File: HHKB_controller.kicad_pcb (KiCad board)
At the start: 2 copper layers, 141.5 x 36 mm, 94 parts, among them CN1 JP, CN2 PRO2, J1 USB_mini_micro_B, P1 GND, P10 CONN_1, P100 LIPO, P11 CONN_1, P110 CONN_1, P111 CONN_1, P112 CONN_1, P113 CONN_1, P114 CONN_1, P115 CONN_1, P12 CONN_1, P13 CONN_1, P14 CONN_1, P15 CONN_1, P2 D+, P3 D-, P4 VUSB, P5 PD1, P6 PD0, P7 GND, P8 CONN_3X2, P9 CONN_1, Q1 Nch, Q10 Nch, Q2 Nch, Q3 Nch, Q4 Pch, Q5 Pch, SW1 SW_PUSH, SW2 SW_DPDT, U1 ATMEGA32U4, U2 MIC5504-3.3YMTR, U3 NCP1402SN50, U4 MCP73832, U5 RN42, X1 16MHz

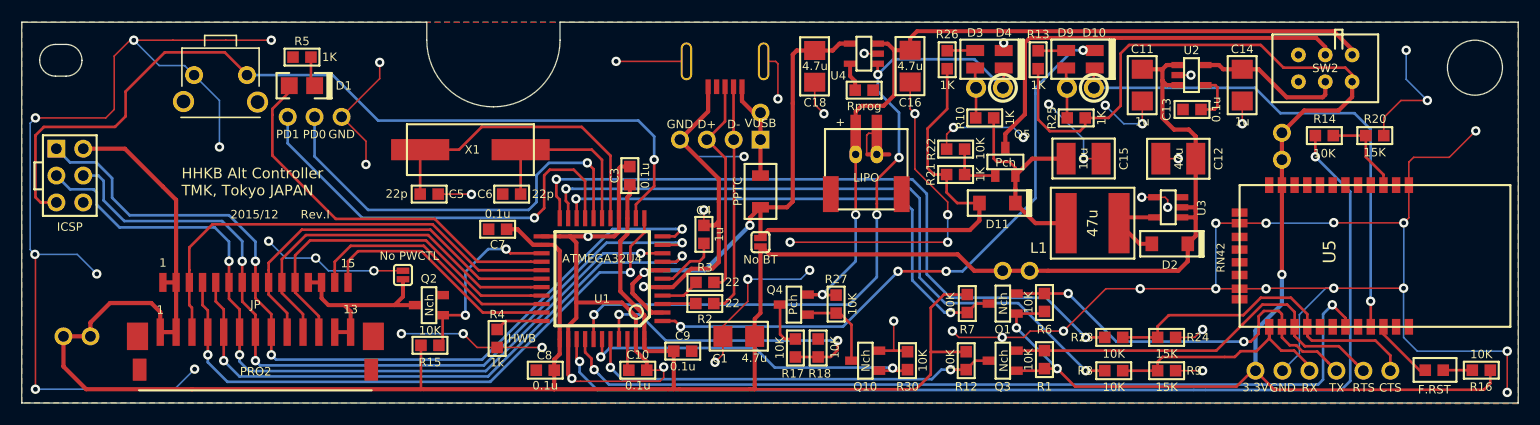
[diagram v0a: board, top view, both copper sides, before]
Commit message: Remove unused C13 of MIC5504 voltage regulator
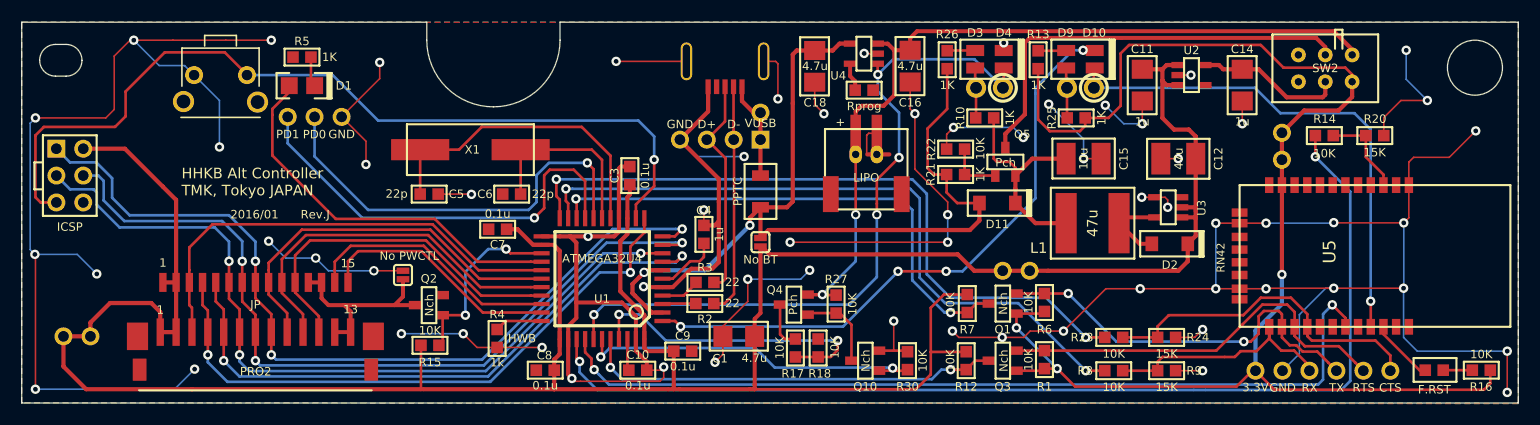
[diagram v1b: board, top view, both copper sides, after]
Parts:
- removed C13: 0.1u, keyboard_parts:C_1608
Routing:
- net Net-(U2-Pad4): track 4.74 -> 0.00 mm
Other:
- board text added: "2016/01"
- board text added: "Rev.J"
- board text removed: "2015/12"
- board text removed: "Rev.I"

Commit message: Add TMK logo
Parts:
- added G***: LOGO, keyboard_parts:tmk2016, B.Cu at (91.8, 110.1)

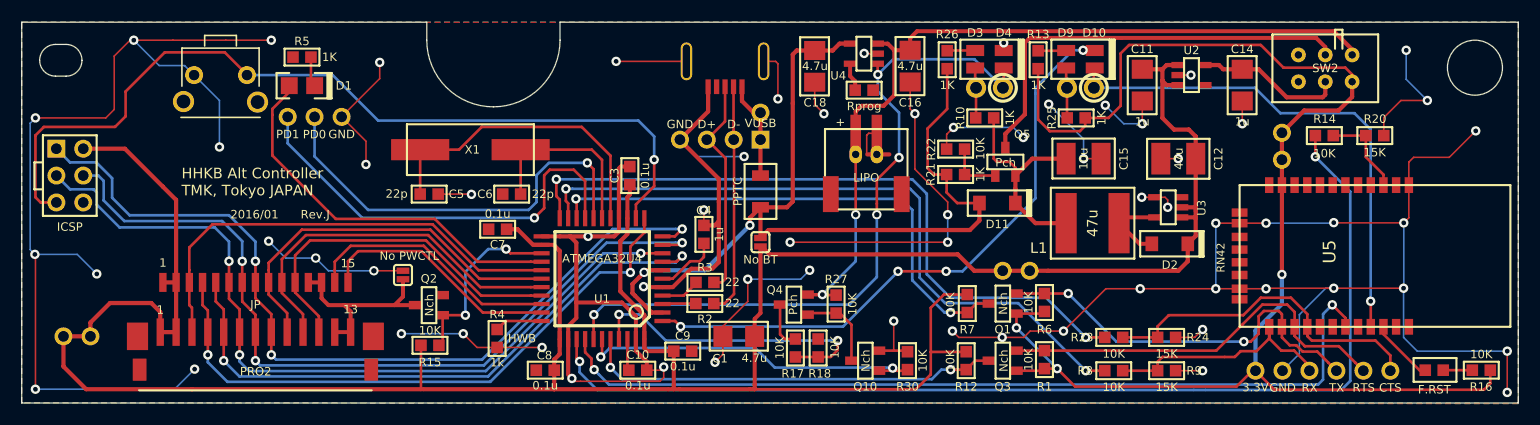
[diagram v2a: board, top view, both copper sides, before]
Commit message: Change foot print of D1 and Add D5
Change pad size of LED(D1) for proper reflow
Add D5 schottky diode for reverse polarity protection
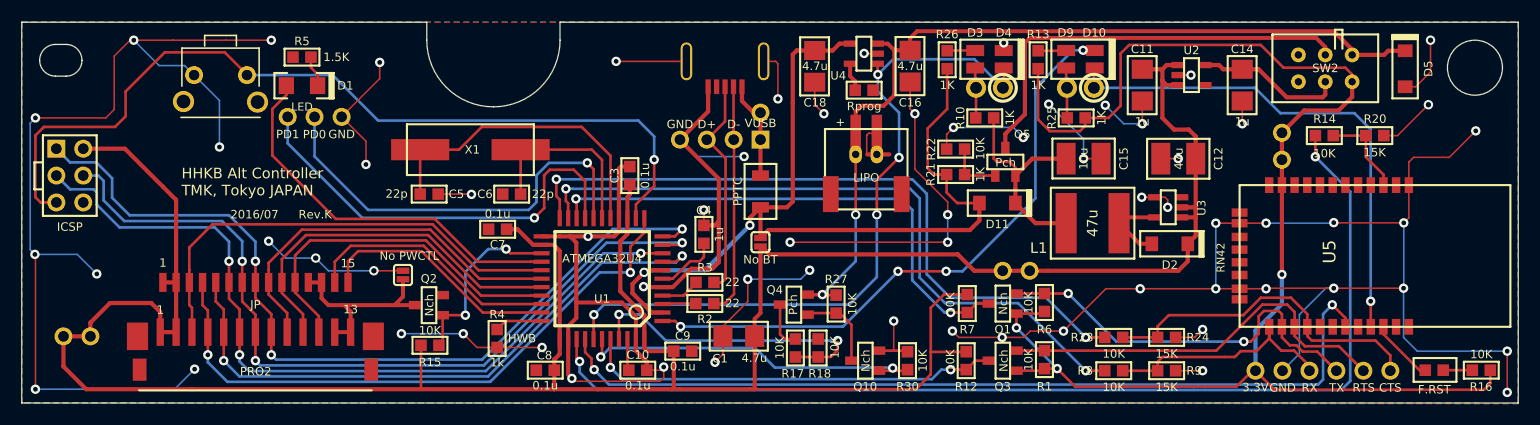
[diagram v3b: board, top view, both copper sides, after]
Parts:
- added D5: D, keyboard_parts:D_SOD123, F.Cu at (207.7, 85.2)
- D1: footprint keyboard_parts:LED_2012_HSOL -> keyboard_parts:LED_3020_REFLOW
- R5: value 1K -> 1.5K
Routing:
- net /bluetooth/LIPO_RAW: track 80.8 -> 86.0 mm
- net GND: track 465.3 -> 464.7 mm
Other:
- board text added: "2016/07"
- board text added: "Rev.K"
- board text removed: "2016/01"
- board text removed: "Rev.J"
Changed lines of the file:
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@@
-(kicad_pcb (version 4) (host pcbnew no-vcs-found-product)
+(kicad_pcb (version 4) (host pcbnew 4.0.2+e4-6225~38~ubuntu16.04.1-stable)
   (general
-    (links 209)
+    (links 211)
     (no_connects 0)
     (area 76.849999 80.749999 218.450001 116.850001)
     (thickness 1.6)
     (drawings 77)
-    (tracks 995)
+    (tracks 999)
     (zones 0)
-    (modules 94)
+    (modules 95)
     (nets 88)
   )
@@
   (title_block
     (title "HHKB Alt Controller")
-    (date 2016/01)
-    (rev J)
+    (date 2016/07)
+    (rev K)
     (company TMK)
   )
   (layers
     (0 F.Cu signal)
-    (31 B.Cu signal)
+    (31 B.Cu signal hide)
     (34 B.Paste user)
     (35 F.Paste user)
@@
   )
   (setup
-    (last_trace_width 0.254)
+    (last_trace_width 0.1524)
     (user_trace_width 0.1524)
     (user_trace_width 0.254)
@@
     (add_net GND)
   )
+  (module keyboard_parts:LED_3020_REFLOW (layer F.Cu)
+    (at 103.4 86.8)
+    (descr "LED 0805 smd package")
+    (tags "LED 0805 SMD")
+    (attr smd)
+    (fp_text reference D1 (at 4.1 0) (layer F.SilkS)
+      (effects (font (size 0.8 0.8) (thickness 0.15)))
+    )
+    (fp_text value LED (at 0 2) (layer F.SilkS)
+      (effects (font (size 0.762 0.762) (thickness 0.127)))
+    )
+    (fp_line (start 2.9 -1.2) (end 2.9 1.2) (layer F.SilkS) (width 0.2))
+    (fp_line (start 2.8 1.2) (end 2.8 -1.2) (layer F.SilkS) (width 0.2))
+    (fp_line (start 2.7 -1.2) (end 2.7 1.2) (layer F.SilkS) (width 0.2))
+    (fp_line (start -1.4 -1.2) (end -2.6 -1.2) (layer F.SilkS) (width 0.2))
+    (fp_line (start -2.6 -1.2) (end -2.6 1.2) (layer F.SilkS) (width 0.2))
+    (fp_line (start -2.6 1.2) (end -1.4 1.2) (layer F.SilkS) (width 0.2))
+    (fp_line (start 2.6 -1.2) (end 2.6 1.2) (layer F.SilkS) (width 0.2))
+    (fp_line (start 1.4 -1.2) (end 3 -1.2) (layer F.SilkS) (width 0.2))
+    (fp_line (start 3 -1.2) (end 3 1.2) (layer F.SilkS) (width 0.2))
+    (fp_line (start 3 1.2) (end 1.4 1.2) (layer F.SilkS) (width 0.2))
+    (pad 1 smd rect (at -1.475 0) (size 1.45 1.6) (layers F.Cu F.Paste F.Mask)
+      (net 19 /PD6))
+    (pad 2 smd rect (at 1.475 0) (size 1.45 1.6) (layers F.Cu F.Paste F.Mask)
+      (net 43 "Net-(D1-Pad2)"))
+  )
   (module keyboard_parts:SOT23-5_HSOL (layer F.Cu)
     (at 185.3 98.3 90)
@@
       (effects (font (size 0.8 0.8) (thickness 0.15)))
     )
-    (fp_text value 1K (at -2.6 0 180) (layer F.SilkS)
+    (fp_text value 1.5K (at -3.25 0 180) (layer F.SilkS)
       (effects (font (size 0.8 0.8) (thickness 0.15)))
     )
@@
       (net 38 GND))
   )
-  (module keyboard_parts:LED_2012_HSOL (layer F.Cu)
-    (at 103.4 86.8)
-    (descr "LED 0805 smd package")
-    (tags "LED 0805 SMD")
-    (attr smd)
-    (fp_text reference D1 (at 3.95 0) (layer F.SilkS)
-      (effects (font (size 0.8 0.8) (thickness 0.15)))
-    )
-    (fp_text value LED (at 0 2) (layer F.SilkS) hide
-      (effects (font (size 0.762 0.762) (thickness 0.127)))
-    )
-    (fp_line (start 2.7 -1.2) (end 2.7 1.2) (layer F.SilkS) (width 0.2))
-    (fp_line (start 2.6 1.2) (end 2.6 -1.2) (layer F.SilkS) (width 0.2))
-    (fp_line (start 2.5 -1.2) (end 2.5 1.2) (layer F.SilkS) (width 0.2))
-    (fp_line (start -1.2 -1.2) (end -2.4 -1.2) (layer F.SilkS) (width 0.2))
-    (fp_line (start -2.4 -1.2) (end -2.4 1.2) (layer F.SilkS) (width 0.2))
-    (fp_line (start -2.4 1.2) (end -1.2 1.2) (layer F.SilkS) (width 0.2))
-    (fp_line (start 2.4 -1.2) (end 2.4 1.2) (layer F.SilkS) (width 0.2))
-    (fp_line (start 1.2 -1.2) (end 2.8 -1.2) (layer F.SilkS) (width 0.2))
-    (fp_line (start 2.8 -1.2) (end 2.8 1.2) (layer F.SilkS) (width 0.2))
-    (fp_line (start 2.8 1.2) (end 1.2 1.2) (layer F.SilkS) (width 0.2))
-    (pad 1 smd rect (at -1.1 0) (size 1.6 1.6) (drill (offset -0.1 0)) (layers F.Cu F.Paste F.Mask)
-      (net 19 /PD6))
-    (pad 2 smd rect (at 1.1 0) (size 1.6 1.6) (drill (offset 0.1 0)) (layers F.Cu F.Paste F.Mask)
-      (net 43 "Net-(D1-Pad2)"))
-  )
   (module keyboard_parts:SOLDER_JUMPER_2 (layer F.Cu)
     (at 146.75 101.6 270)
@@
       (xy 5.948572 0.536514) (xy 6.045721 0.383371) (xy 6.084519 0.266973) (xy 6.084519 0.266973)) (layer B.SilkS) (width 0.1))
   )
+  (module keyboard_parts:D_SOD123 (layer F.Cu)
+    (at 207.7 85.2 270)
+    (fp_text reference D5 (at 0 -2.2 450) (layer F.SilkS)
+      (effects (font (size 0.8 0.8) (thickness 0.15)))
+    )
+    (fp_text value D (at 0 -1.925 270) (layer F.SilkS) hide
+      (effects (font (size 0.8 0.8) (thickness 0.15)))
+    )
+    (fp_line (start -3.075 1.2) (end -3.075 -1.2) (layer F.SilkS) (width 0.2))
+    (fp_line (start -2.8 -1.2) (end -2.8 1.2) (layer F.SilkS) (width 0.2))
+    (fp_line (start -2.925 -1.2) (end -2.925 1.2) (layer F.SilkS) (width 0.2))
+    (fp_line (start -3.2 -1.2) (end 2.8 -1.2) (layer F.SilkS) (width 0.2))
+    (fp_line (start 2.8 -1.2) (end 2.8 1.2) (layer F.SilkS) (width 0.2))
+    (fp_line (start 2.8 1.2) (end -3.2 1.2) (layer F.SilkS) (width 0.2))
+    (fp_line (start -3.2 1.2) (end -3.2 -1.2) (layer F.SilkS) (width 0.2))
+    (pad 1 smd rect (at 1.7 0 270) (size 1.2 1.4) (layers F.Cu F.Paste F.Mask)
+      (net 38 GND))
+    (pad 2 smd rect (at -1.7 0 270) (size 1.2 1.4) (layers F.Cu F.Paste F.Mask)
+      (net 25 /bluetooth/LIPO_RAW))
+  )
   (dimension 5.2 (width 0.15) (layer Dwgs.User)
     (gr_text "5.200 mm" (at 220.91 85.1 270) (layer Dwgs.User)
@@
     (arrow2b (pts (xy 207.4 73) (xy 208.526504 72.413579)))
   )
-  (gr_text Rev.J (at 104.65 98.98) (layer F.SilkS)
+  (gr_text Rev.K (at 104.65 98.98) (layer F.SilkS)
     (effects (font (size 0.8 0.8) (thickness 0.15)))
   )
-  (gr_text 2016/01 (at 98.91 98.98) (layer F.SilkS)
+  (gr_text 2016/07 (at 98.91 98.98) (layer F.SilkS)
     (effects (font (size 0.8 0.8) (thickness 0.15)))
   )
@@
   (segment (start 116.7 111) (end 116.35 111.35) (width 0.254) (layer F.Cu) (net 18))
   (segment (start 116.7 108.5) (end 116.7 111) (width 0.254) (layer F.Cu) (net 18))
-  (segment (start 102.3 86.8) (end 102.3 87.3) (width 0.254) (layer F.Cu) (net 19))
-  (segment (start 102.3 87.3) (end 100.6 89) (width 0.254) (layer F.Cu) (net 19))
+  (segment (start 101.925 86.8) (end 101.925 87.675) (width 0.254) (layer F.Cu) (net 19))
+  (segment (start 101.925 87.675) (end 100.6 89) (width 0.254) (layer F.Cu) (net 19))
   (segment (start 100.6 89) (end 100.6 89.554) (width 0.254) (layer F.Cu) (net 19))
   (segment (start 106.6 99.4) (end 115.960604 99.4) (width 0.254) (layer F.Cu) (net 19))
@@
   (segment (start 178.27 85.205) (end 178.35 85.125) (width 0.254) (layer F.Cu) (net 24))
   (segment (start 178.27 87) (end 178.27 85.205) (width 0.254) (layer F.Cu) (net 24))
+  (segment (start 206.1 83.5) (end 207.7 83.5) (width 0.4) (layer F.Cu) (net 25))
+  (segment (start 205.71 83.89) (end 206.1 83.5) (width 0.4) (layer F.Cu) (net 25))
+  (segment (start 202.69 83.89) (end 205.71 83.89) (width 0.4) (layer F.Cu) (net 25))
   (segment (start 155.75 93.3) (end 155.75 91.3) (width 0.381) (layer F.Cu) (net 25))
   (segment (start 159.4 83.45) (end 160.9 83.45) (width 0.381) (layer F.Cu) (net 25))
@@
   (segment (start 166.3 108.25) (end 167.15 107.4) (width 0.254) (layer F.Cu) (net 37))
   (segment (start 167.15 107.4) (end 168.35 107.4) (width 0.254) (layer F.Cu) (net 37))
+  (segment (start 205.68 91.52) (end 206.98 91.52) (width 0.1524) (layer F.Cu) (net 38))
+  (via (at 209.9 88.6) (size 0.889) (drill 0.508) (layers F.Cu B.Cu) (net 38))
+  (segment (start 206.98 91.52) (end 209.9 88.6) (width 0.1524) (layer F.Cu) (net 38))
+  (segment (start 207.7 86.9) (end 208.7 86.9) (width 0.1524) (layer F.Cu) (net 38))
+  (via (at 210.1 82.5) (size 0.889) (drill 0.508) (layers F.Cu B.Cu) (net 38))
+  (segment (start 210.1 85.5) (end 210.1 82.5) (width 0.1524) (layer F.Cu) (net 38))
+  (segment (start 208.7 86.9) (end 210.1 85.5) (width 0.1524) (layer F.Cu) (net 38))
   (segment (start 147.05 84.5) (end 148.18 84.5) (width 0.1524) (layer F.Cu) (net 38))
   (via (at 148.4 88.05) (size 0.889) (layers F.Cu B.Cu) (net 38))
@@
   (via (at 185.25 98.3) (size 0.889) (layers F.Cu B.Cu) (net 38))
   (segment (start 184 97.35) (end 185 97.35) (width 0.1524) (layer F.Cu) (net 38))
-  (segment (start 205.68 89.82) (end 207.3 88.2) (width 0.1524) (layer F.Cu) (net 38))
-  (segment (start 207.3 88.2) (end 209.8 88.2) (width 0.1524) (layer F.Cu) (net 38))
-  (via (at 209.8 88.2) (size 0.889) (layers F.Cu B.Cu) (net 38))
-  (segment (start 209.8 88.2) (end 207.8 86.2) (width 0.1524) (layer B.Cu) (net 38))
-  (segment (start 207.8 86.2) (end 207.8 83.45) (width 0.1524) (layer B.Cu) (net 38))
-  (via (at 207.8 83.45) (size 0.889) (layers F.Cu B.Cu) (net 38))
-  (segment (start 205.68 91.52) (end 205.68 89.82) (width 0.1524) (layer F.Cu) (net 38))
   (segment (start 143.2 110.5) (end 143.2 109.55) (width 0.1524) (layer F.Cu) (net 38))
   (segment (start 156.575 83.775) (end 156.55 83.75) (width 0.1524) (layer F.Cu) (net 38))
@@
   (segment (start 130.8 92.85) (end 124.075 92.85) (width 0.254) (layer F.Cu) (net 42))
   (segment (start 131.77 99.333) (end 131.77 93.82) (width 0.254) (layer F.Cu) (net 42))
-  (segment (start 104.25 86.55) (end 104.5 86.8) (width 0.254) (layer F.Cu) (net 43))
-  (segment (start 104.25 84.1) (end 104.25 86.55) (width 0.254) (layer F.Cu) (net 43))
+  (segment (start 104.875 86.8) (end 104.875 85.725) (width 0.254) (layer F.Cu) (net 43))
+  (segment (start 104.25 85.1) (end 104.25 84.1) (width 0.254) (layer F.Cu) (net 43))
+  (segment (start 104.875 85.725) (end 104.25 85.1) (width 0.254) (layer F.Cu) (net 43))
   (segment (start 181.2 99.25) (end 180.65 99.8) (width 0.381) (layer F.Cu) (net 44))
   (segment (start 184 99.25) (end 181.2 99.25) (width 0.381) (layer F.Cu) (net 44))

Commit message: Enlarge TH land of USB connector
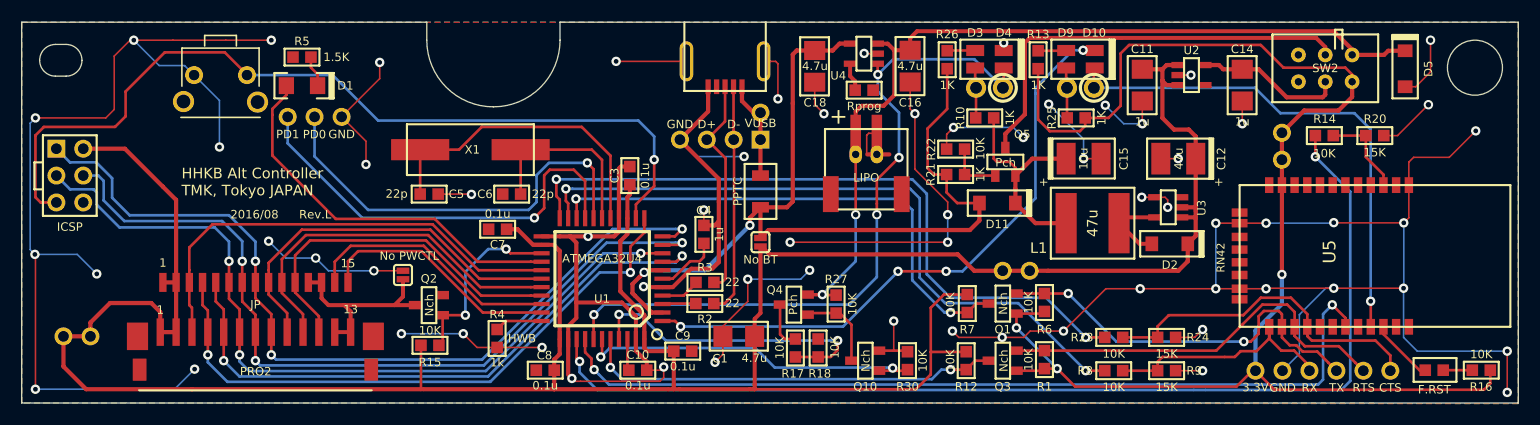
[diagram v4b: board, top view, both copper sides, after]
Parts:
- J1: footprint keyboard_parts:USB_miniB_hirose_5S8 -> USB_miniB_hirose_5S8
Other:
- board text added: "2016/08"
- board text added: "Rev.L"
- board text removed: "2016/07"
- board text removed: "Rev.K"

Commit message: Change LED, USB connector and TACT switch(Rev.M)
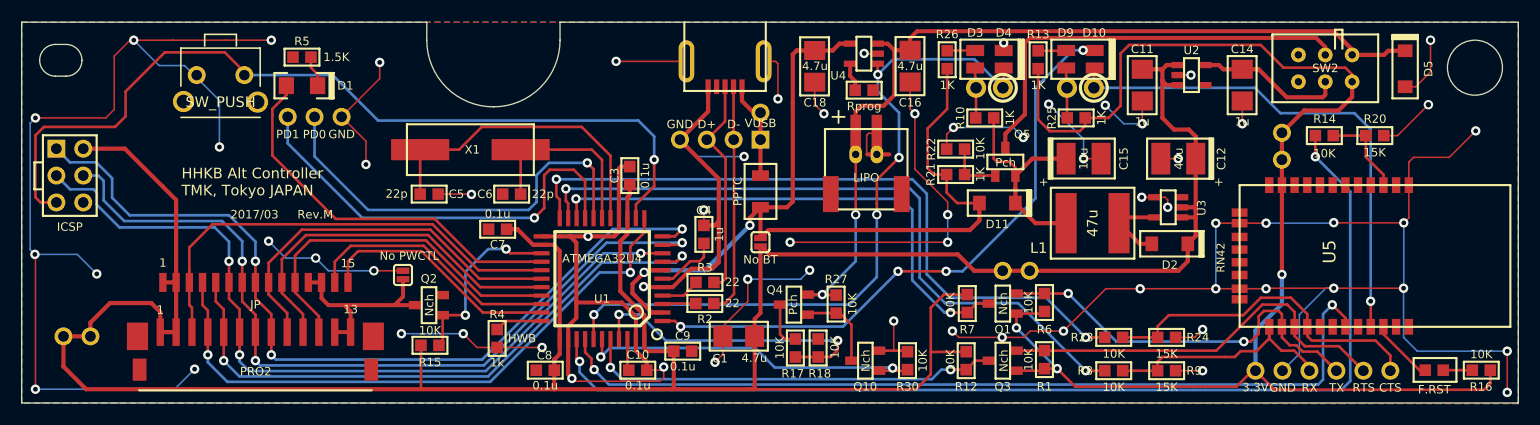
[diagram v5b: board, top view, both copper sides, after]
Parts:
- SW1: footprint keyboard_parts:SW_TACT_TH_HORIZ_LOW -> keyboard_parts:SW_TACT_TH_HORIZ
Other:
- board text added: "2017/03"
- board text added: "Rev.M"
- board text removed: "2016/08"
- board text removed: "Rev.L"
